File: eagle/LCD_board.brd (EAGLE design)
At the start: 160 x 100 mm, 5 parts, among them CN1 1X4-CLEANBIG

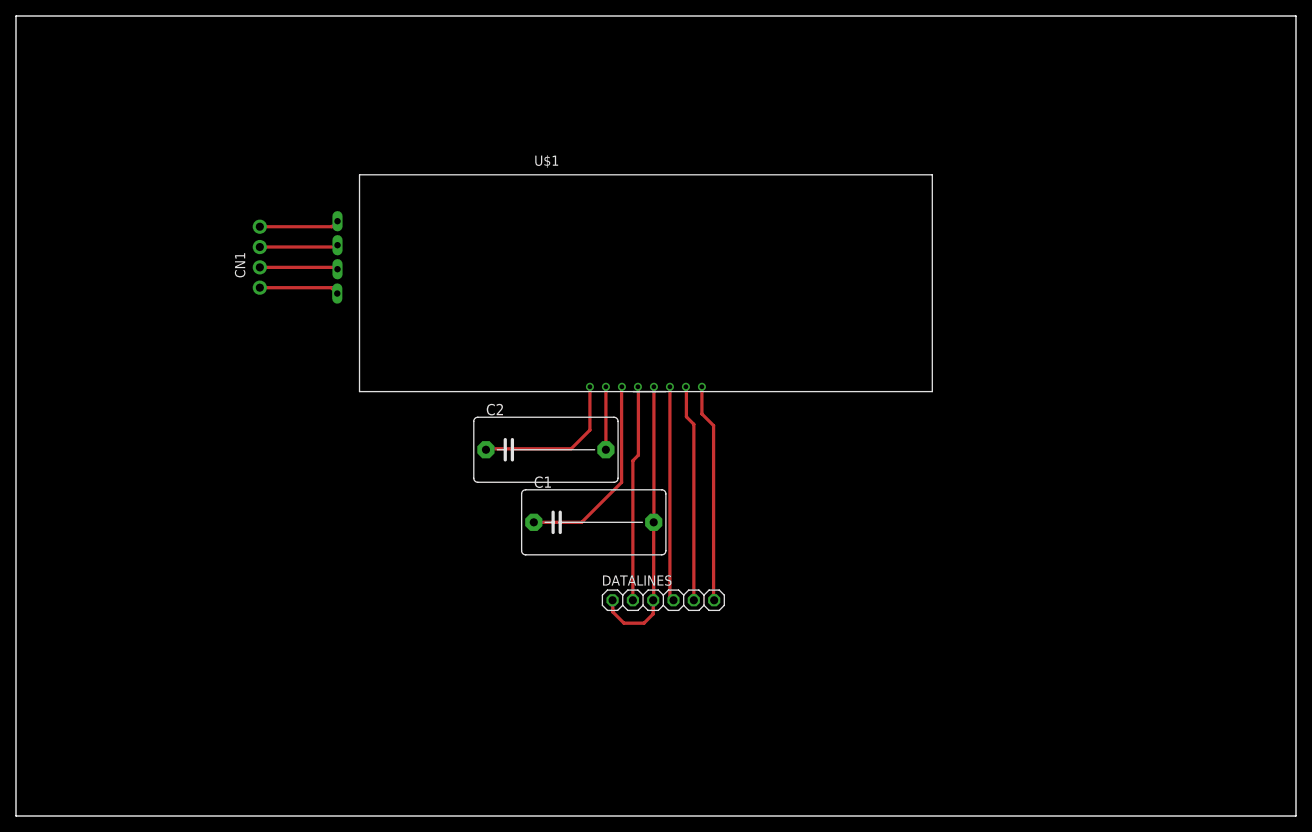
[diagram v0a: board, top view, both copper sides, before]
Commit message: LCD board with pull up resistor
This should give us a working screen with thru hole components just to
check dimensions and use for debug. Next change resistor and capacitor
for surface mount and determine if RGB resistors will be on this or the
main board.
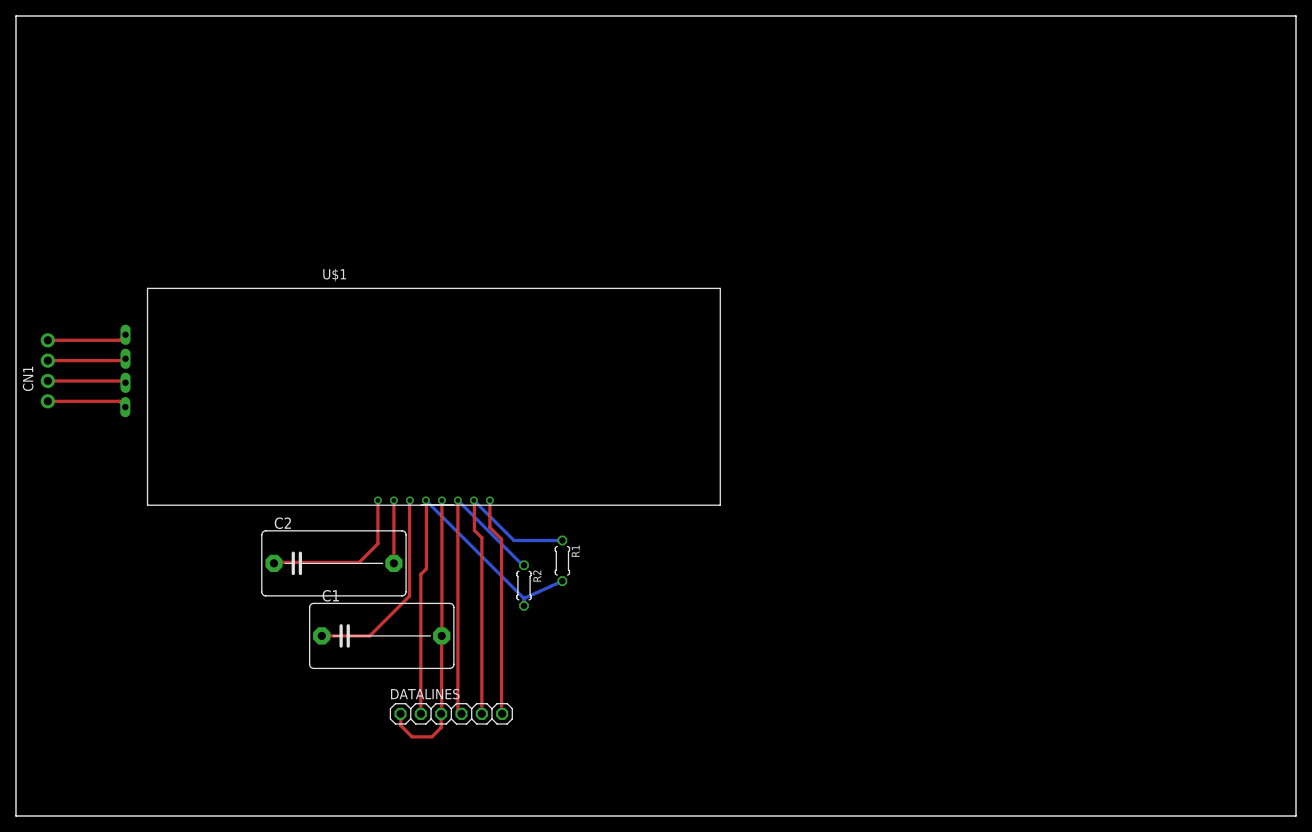
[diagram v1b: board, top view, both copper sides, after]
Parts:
- added R1, R2: 4.7k, LockBox:0204/5
- moved C1 30.1 mm to (45.7, 22.5)
- moved CN1 30.1 mm to (3.98, 55.6)
- moved DATALINES 30.1 mm to (54.4, 12.8)
- moved C2 30.1 mm to (39.7, 31.6)
- moved U$1 30.1 mm to (52.2, 55.6)
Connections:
- net SCL: now also R1.1
- net SDA: now also R2.1
- net VDD: now also R1.2, R2.2
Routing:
- net VDD: track 27.0 -> 50.5 mm
- net SCL: track 27.1 -> 40.2 mm
- net SDA: track 26.9 -> 38.5 mm
